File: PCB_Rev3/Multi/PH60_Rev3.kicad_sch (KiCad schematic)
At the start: 49 parts, among them J1 Conn_01x02_Pin, J2 Conn_01x02_Pin, J3 USB_C_Receptacle_USB2.0_16P, J4 Conn_01x04_Socket, U2 nRF52840, U4 LGS5500EP, X1 32.768kHz, X2 Crystal_Generic

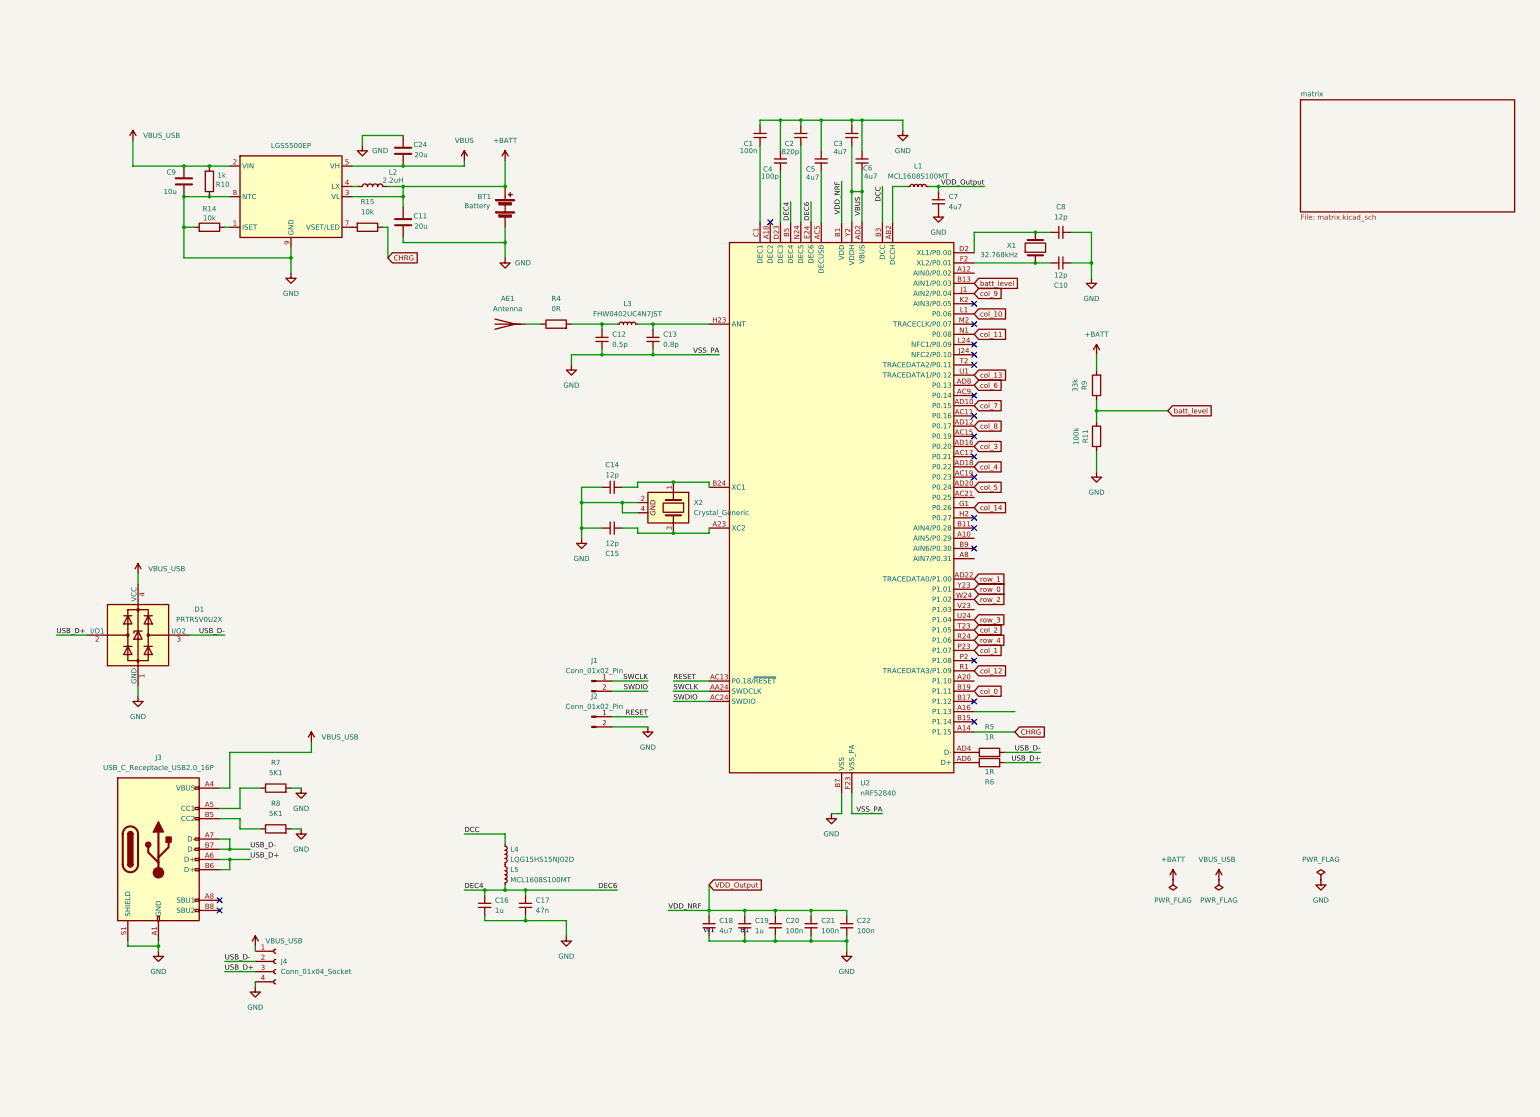
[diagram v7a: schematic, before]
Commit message: Change charger and power supply
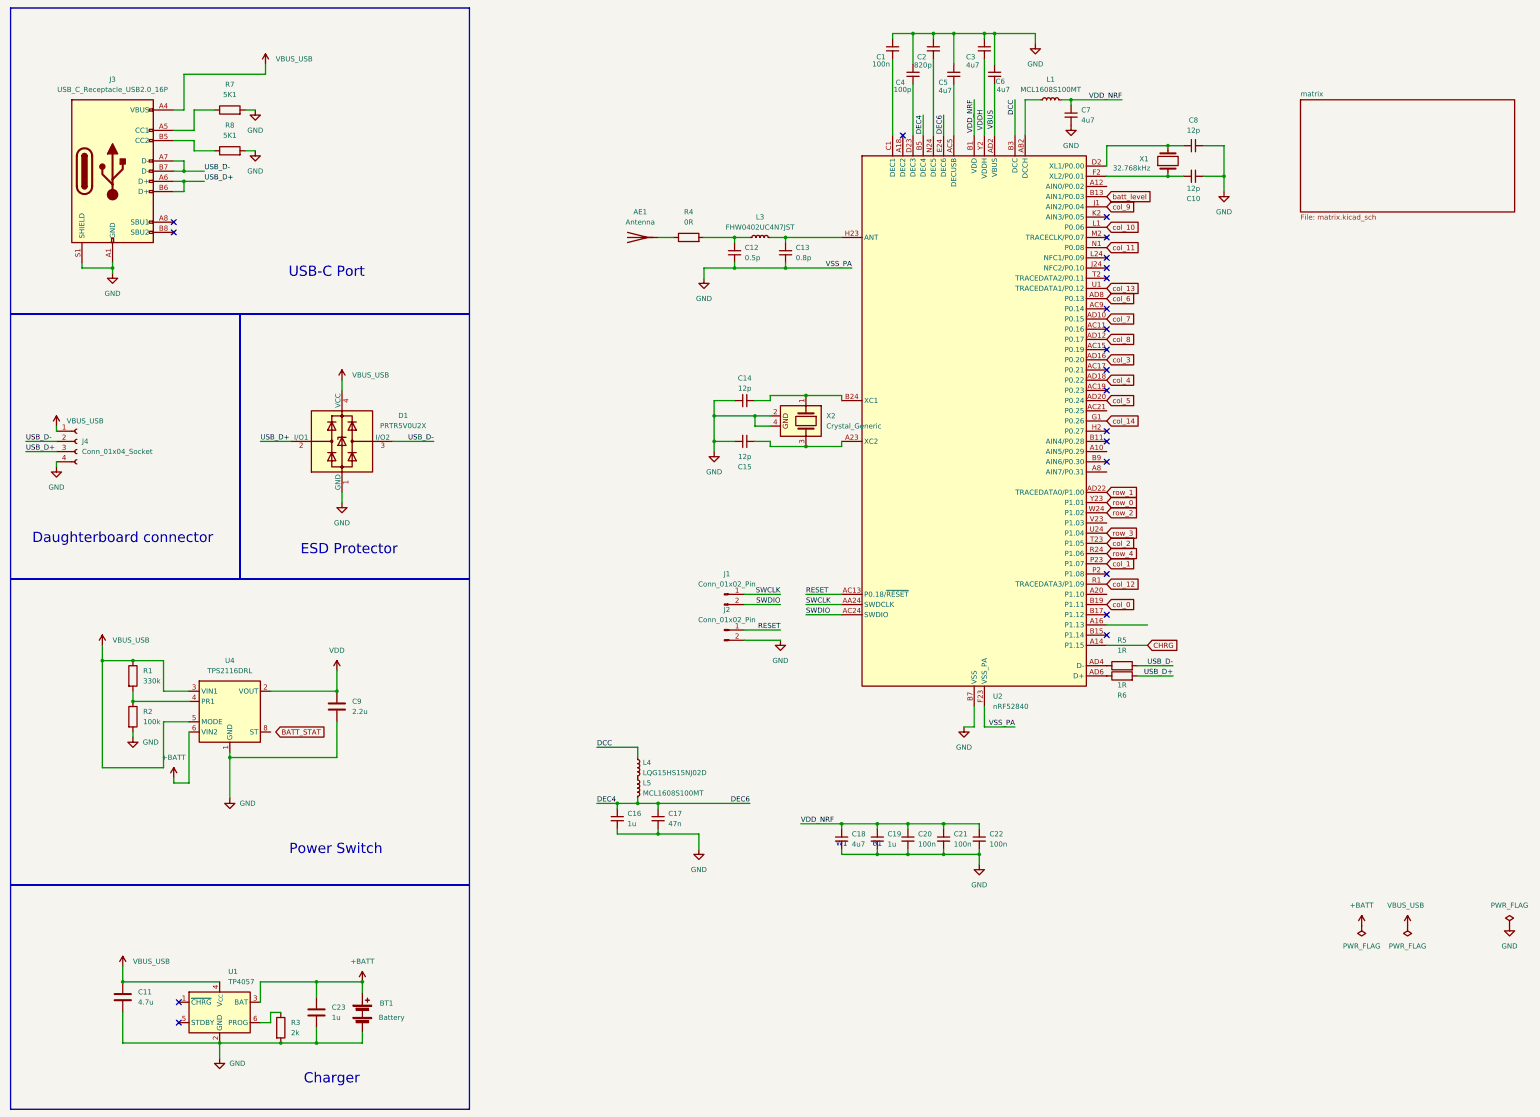
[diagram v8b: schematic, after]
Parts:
- removed C24: 20u, Capacitor_SMD:C_0402_1005Metric, symbol Device:C
- removed L2: 2.2uH, Inductor_SMD:L_Changjiang_FNR252012S, symbol Device:L
- removed R10: 1k, PCM_Resistor_SMD_AKL:R_0402_1005Metric, symbol Device:R
- removed R11: 100k, PCM_Resistor_SMD_AKL:R_0402_1005Metric, symbol Device:R
- removed R14, R15: 10k, PCM_Resistor_SMD_AKL:R_0402_1005Metric, symbol Device:R
- removed R9: 33k, PCM_Resistor_SMD_AKL:R_0402_1005Metric, symbol Device:R
- removed U4: LGS5500EP, Package_SO:SOIC-8-1EP_3.9x4.9mm_P1.27mm_EP2.41x3.3mm, symbol Battery_Management:LGS5500EP
- added C23: 1u, symbol Device:C
- added R1: 330k, symbol Device:R
- added R2: 100k, symbol Device:R
- added R3: 2k, symbol Device:R
- added U1: TP4057, Package_TO_SOT_SMD:TSOT-23-6, symbol Battery_Management:TP4057
- added U4: TPS2116DRL, Package_TO_SOT_SMD:SOT-583-8, symbol Power_Management:TPS2116DRL
- C11: value 20u -> 4.7u; footprint Capacitor_SMD:C_0402_1005Metric -> (none)
- C9: value 10u -> 2.2u; footprint Capacitor_SMD:C_0402_1005Metric -> (none)
- J4: footprint Connector_FFC-FPC:Molex_200528-0040_1x04-1MP_P1.00mm_Horizontal -> Connector_Molex:Molex_Pico-EZmate_78171-0004_1x04-1MP_P1.20mm_Vertical
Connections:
- net +BATT: now also C23.1, U1.3 (BAT), U4.6 (VIN2); no longer C11.1
- net GND: now also C23.2, R2.2, R3.2, U1.2 (GND), U4.1 (GND)
- net VBUS: no longer C3.2, U2.Y2 (VDDH)
- net VBUS_USB: now also C11.1, R1.1, U1.4 (V_{CC}), U4.3 (VIN1), U4.5 (MODE); no longer C9.1
- net VDD_Output renamed VDD_NRF
- new net: R3.1, U1.6 (PROG)
- new net: R1.2, R2.1, U4.4 (PR1)
- new net VDD: C9.1, U4.2 (VOUT), U4.7 (VOUT)
- new net VDDH: C3.2, U2.Y2 (VDDH)
- no-connect marks 19 -> 21
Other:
- note added: "Charger"
- note added: "Daughterboard connector"
- note added: "ESD Protector"
- note added: "Power Switch"
- note added: "USB-C Port"
- moved on the sheet: AE1, BT1, C1, C10, C12, C13, C14, C15, C16, C17, C18, C19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
